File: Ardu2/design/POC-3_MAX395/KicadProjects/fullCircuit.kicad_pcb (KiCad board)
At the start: 2 copper layers, 189.2 x 143.5 mm, 128 parts, among them P1 CONN_01X02, P7 CONN_01X15, U1 Pyboard, U10 MAX395, U11 MAX395, U12 MAX395, U13 MAX395, U14 MAX395, U15 MAX395, U16 MAX395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

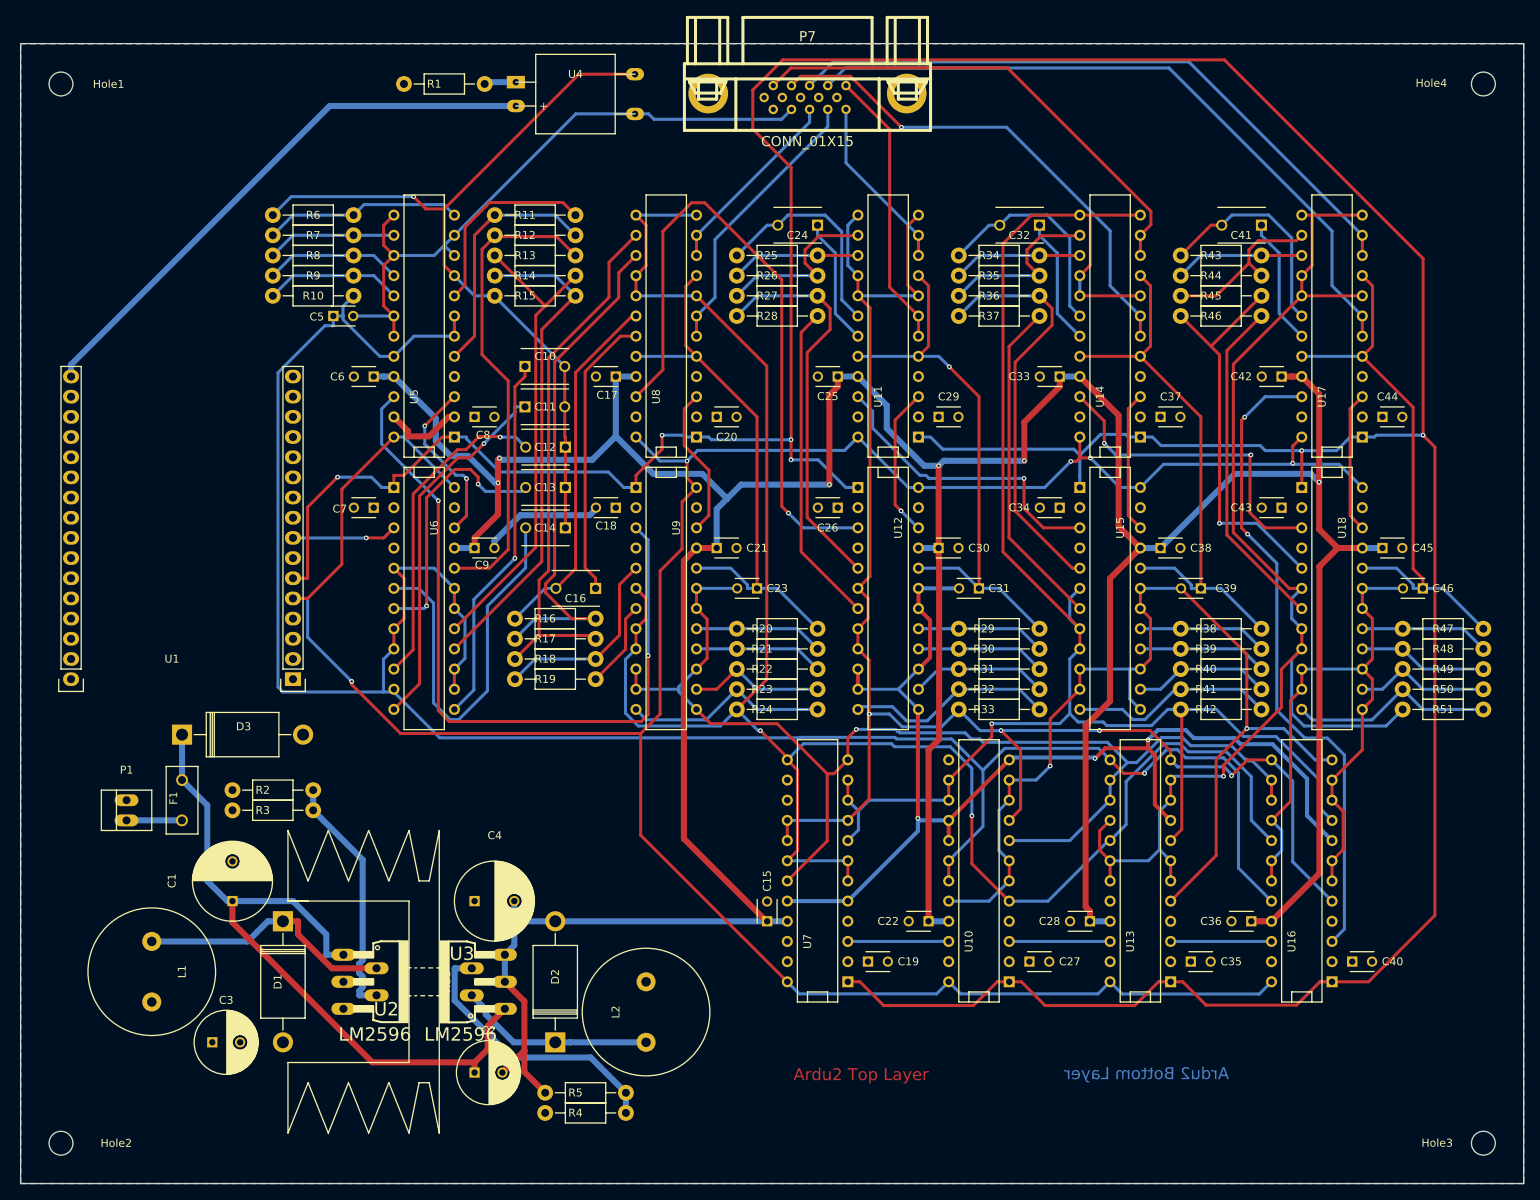
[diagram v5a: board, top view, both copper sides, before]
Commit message: updates to circuit with SENSEI
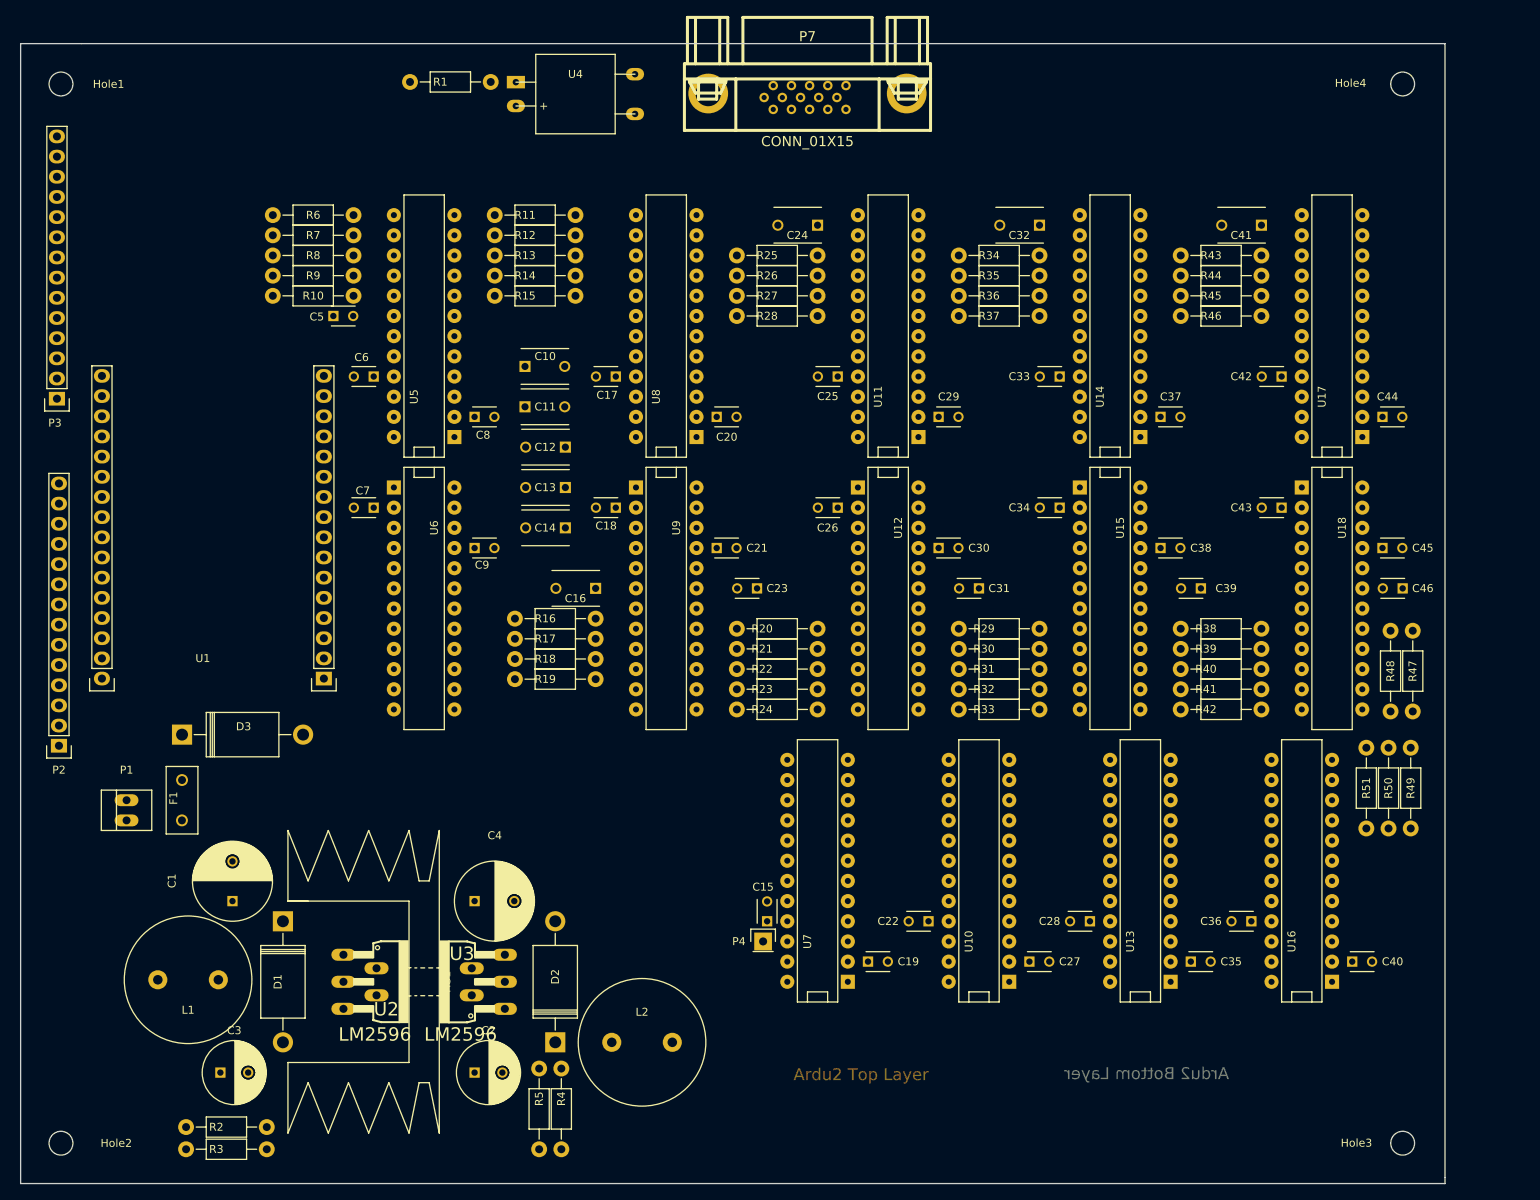
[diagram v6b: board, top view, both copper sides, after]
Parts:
- added P2: CONN_01X14, Pin_Headers:Pin_Header_Straight_1x14, F.Cu at (67.1, 106.2)
- added P3: CONN_01X14, Pin_Headers:Pin_Header_Straight_1x14, F.Cu at (66.8, 62.5)
- added P4: CONN_01X01, Pin_Headers:Pin_Header_Straight_1x01, F.Cu at (155.7, 130.8)
- U10, U11, U12, U13, U14, U15, U16, U17, U18, U5, U6, U7, U8, U9: footprint Housings_DIP:DIP-24__300 -> 330L:DIP-24__300_pads_70_10
- moved R3 43.1 mm to (88.1, 157.0)
- moved R2 42.8 mm to (88.1, 154.2)
- moved R49 15.5 mm to (237.2, 111.5), turned to 90 degrees
- moved R50 14.2 mm to (234.4, 111.5), turned to 90 degrees
- moved R51 13.8 mm to (231.6, 111.5), turned to 90 degrees
- moved Hole3 10.2 mm to (236.2, 156.2)
- moved Hole4 10.2 mm to (236.2, 22.9)
- moved R48 7.17 mm to (234.7, 96.8), turned to 90 degrees
- moved R47 6.55 mm to (237.5, 96.8), turned to 90 degrees
- moved R5 6.19 mm to (127.5, 151.9), turned to 90 degrees
- moved L1 4.68 mm to (83.3, 135.6), turned to 180 degrees
- moved C3 3.94 mm to (87.4, 147.3)
- moved U1 3.89 mm to (85.2, 97.7)
- moved L2 3.84 mm to (140.5, 143.5), turned to 0 degrees
- moved R4 3.09 mm to (130.3, 151.9), turned to 270 degrees
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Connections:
- U1 pad 1: (no net) -> Net-(P2-Pad2)
- U1 pad 10: (no net) -> Net-(P3-Pad8)
- U1 pad 11: (no net) -> Net-(P3-Pad9)
- U1 pad 12: (no net) -> Net-(P3-Pad10)
- U1 pad 13: (no net) -> Net-(P3-Pad11)
- U1 pad 15: (no net) -> /3V3
- U1 pad 18: (no net) -> Net-(P2-Pad13)
- U1 pad 19: (no net) -> Net-(P2-Pad12)
- U1 pad 2: (no net) -> Net-(P2-Pad1)
- U1 pad 20: (no net) -> Net-(P2-Pad11)
- U1 pad 21: (no net) -> Net-(P2-Pad10)
- U1 pad 22: (no net) -> Net-(P2-Pad9)
- U1 pad 23: (no net) -> Net-(P2-Pad8)
- U1 pad 24: (no net) -> Net-(P2-Pad7)
- U1 pad 25: (no net) -> Net-(P2-Pad6)
- U1 pad 26: (no net) -> Net-(P2-Pad5)
- U1 pad 27: (no net) -> Net-(P2-Pad4)
- U1 pad 28: (no net) -> Net-(P2-Pad3)
- U1 pad 29: (no net) -> Net-(U1-Pad29)
- U1 pad 3: (no net) -> Net-(P3-Pad1)
- U1 pad 31: (no net) -> Net-(U1-Pad31)
- U1 pad 4: (no net) -> Net-(P3-Pad2)
- U1 pad 7: (no net) -> Net-(P3-Pad5)
- U1 pad 9: (no net) -> Net-(P3-Pad7)
- U7 pad 22: (no net) -> /DoutSpare
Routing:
- net /V-: track 532.3 -> 0.00 mm, vias 6 -> 0
- net /CLK: track 483.7 -> 0.00 mm, vias 6 -> 0
- net /CS: track 340.8 -> 0.00 mm, vias 5 -> 0
- net /MIn+: track 278.4 -> 0.00 mm, vias 1 -> 0
- net /DOut-: track 246.4 -> 0.00 mm, vias 2 -> 0
- net /BOut-: track 209.3 -> 0.00 mm, vias 1 -> 0
- net /COut-: track 201.5 -> 0.00 mm, vias 4 -> 0
- net /AOut-: track 160.0 -> 0.00 mm, vias 1 -> 0
- net /DOut+: track 154.7 -> 0.00 mm, vias 1 -> 0
- net /COut+: track 145.7 -> 0.00 mm, vias 3 -> 0
- net /BOut+: track 130.8 -> 0.00 mm, vias 2 -> 0
- net GND: track 118.0 -> 0.00 mm, vias 1 -> 0
- net Net-(U5-Pad22): track 94.6 -> 0.00 mm, vias 2 -> 0
- net /BATin: track 92.3 -> 0.00 mm
- net /A+: track 87.7 -> 0.00 mm
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- removed copper zone on B.Cu, net /V+
- removed copper zone on F.Cu, net GND
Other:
- board size 189.2 x 143.5 mm -> 179.3 x 143.5 mm
- net class PSUFeedback added: clearance 0.508, trace_width 0.508, via_dia 0.6, via_drill 0.4
- net class Power: trace_width 0.762 -> 1.905

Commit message: updates after circuit review with SENSEI
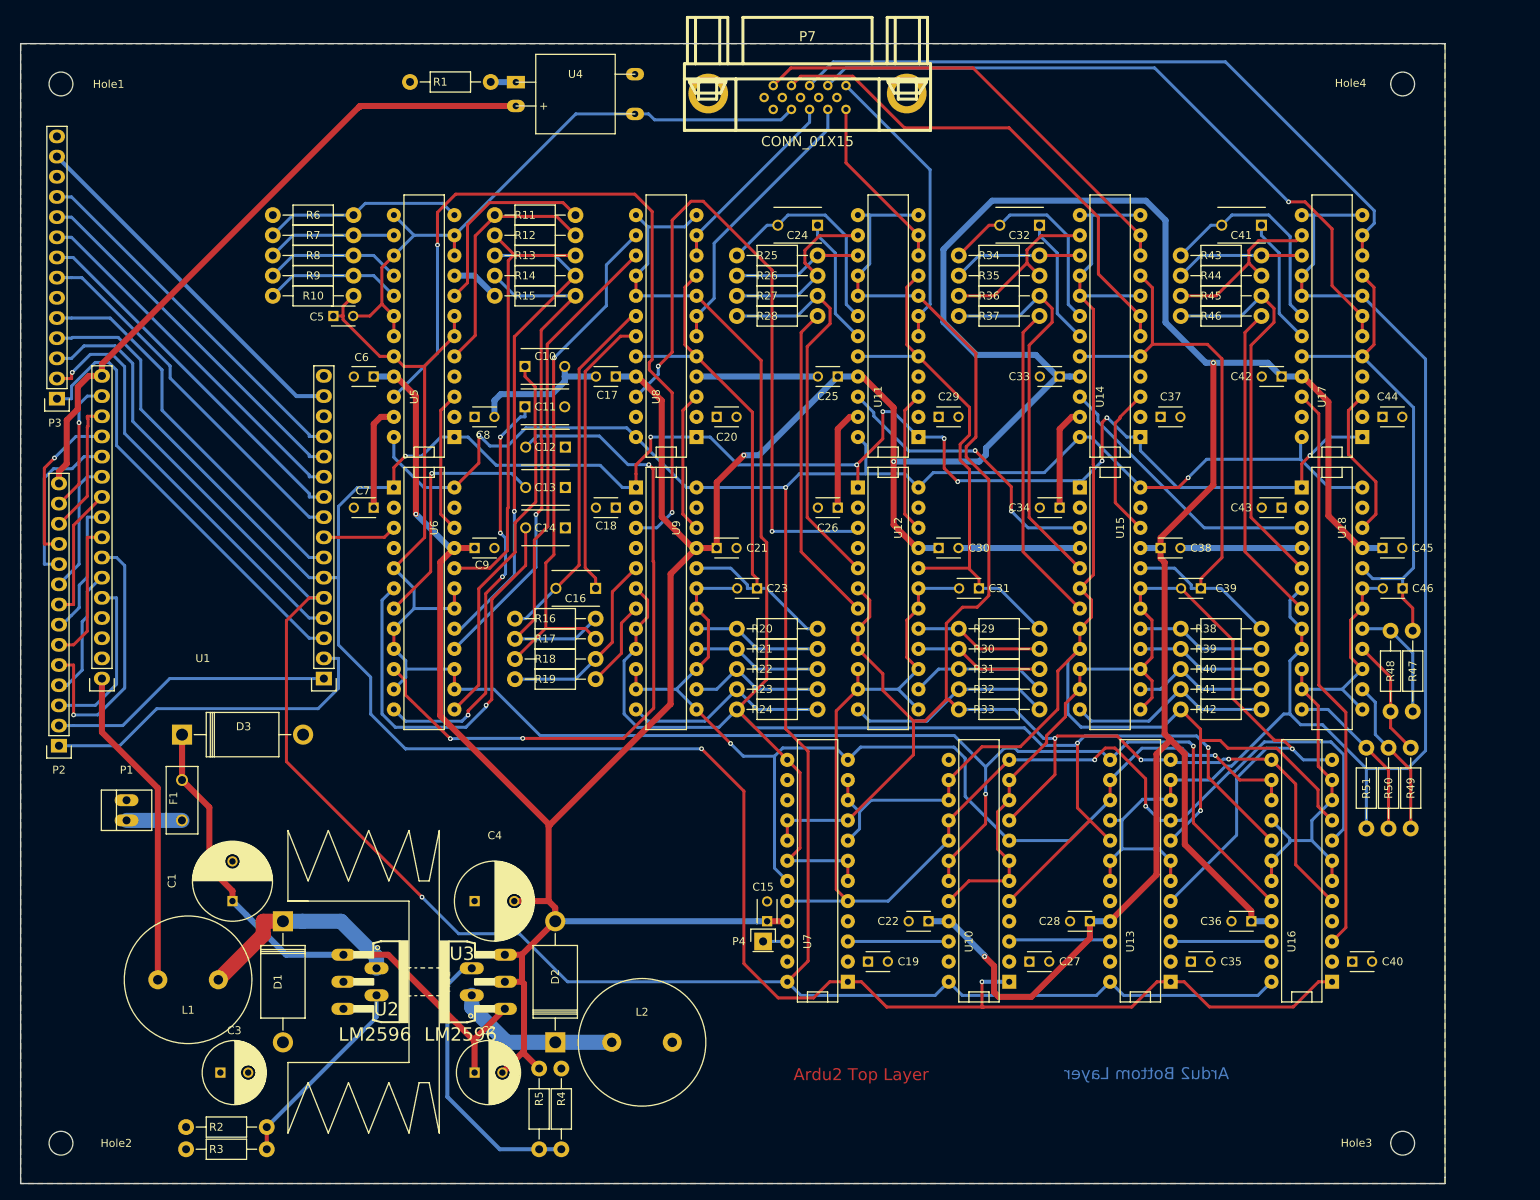
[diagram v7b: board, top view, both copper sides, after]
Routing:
- net /V-: track 0.00 -> 568.9 mm, vias 0 -> 5
- net /CS: track 0.00 -> 432.6 mm, vias 0 -> 4
- net /CLK: track 0.00 -> 414.1 mm, vias 0 -> 11
- net /DOut-: track 0.00 -> 255.4 mm, vias 0 -> 2
- net /MIn+: track 0.00 -> 226.9 mm, vias 0 -> 2
- net /COut-: track 0.00 -> 215.3 mm, vias 0 -> 3
- net /BOut-: track 0.00 -> 188.2 mm, vias 0 -> 1
- net /AOut-: track 0.00 -> 179.9 mm
- net /COut+: track 0.00 -> 161.3 mm, vias 0 -> 2
- net /DOut+: track 0.00 -> 142.4 mm, vias 0 -> 2
- net /BOut+: track 0.00 -> 130.4 mm, vias 0 -> 1
- net Net-(U5-Pad22): track 0.00 -> 98.9 mm, vias 0 -> 2
- net /A+: track 0.00 -> 87.9 mm, vias 0 -> 1
- net Net-(C12-Pad2): track 0.00 -> 87.4 mm, vias 0 -> 3
- net /A-: track 0.00 -> 86.3 mm
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- added copper zone on B.Cu, net /V+
- added copper zone on F.Cu, net GND

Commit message: tweaked PCB tracks, added labels
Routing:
- net /CS: track 432.6 -> 433.9 mm
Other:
- board text added: "**"
- board text added: "3v3"
- board text added: "B- B+ A- A+ C+ G G G G G G O+ D- D+ C-"
- board text added: "Bat+"
- board text added: "Bat-"
- board text added: "DoutSpare"
- board text added: "GND"
- board text added: "RST"
- board text added: "V+"
- board text added: "X1"
- board text added: "X10"
- board text added: "X11"
- board text added: "X12"
- board text added: "X2"
- board text added: "X3"
- board text added: "X4"
- board text added: "X5"
- board text added: "X6"
- board text added: "X7"
- board text added: "Y1"
- board text added: "Y10"
- board text added: "Y11"
- board text added: "Y12"
- board text added: "Y2"
- board text added: "Y3"
- board text added: "Y4"
- board text added: "Y5"
- board text added: "Y6"
- board text added: "Y7"
- board text added: "Y8"
- board text added: "Y9"
